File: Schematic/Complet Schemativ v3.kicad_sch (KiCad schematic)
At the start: 49 parts, among them J1 Conn_Coaxial, J2 USB_A, J3 AudioJack3, U1 Si5351A-B-GT, U2 SN74CBT3253, U3 OPAMP, U4 OPAMP, U5 OPAMP, U6 OPAMP

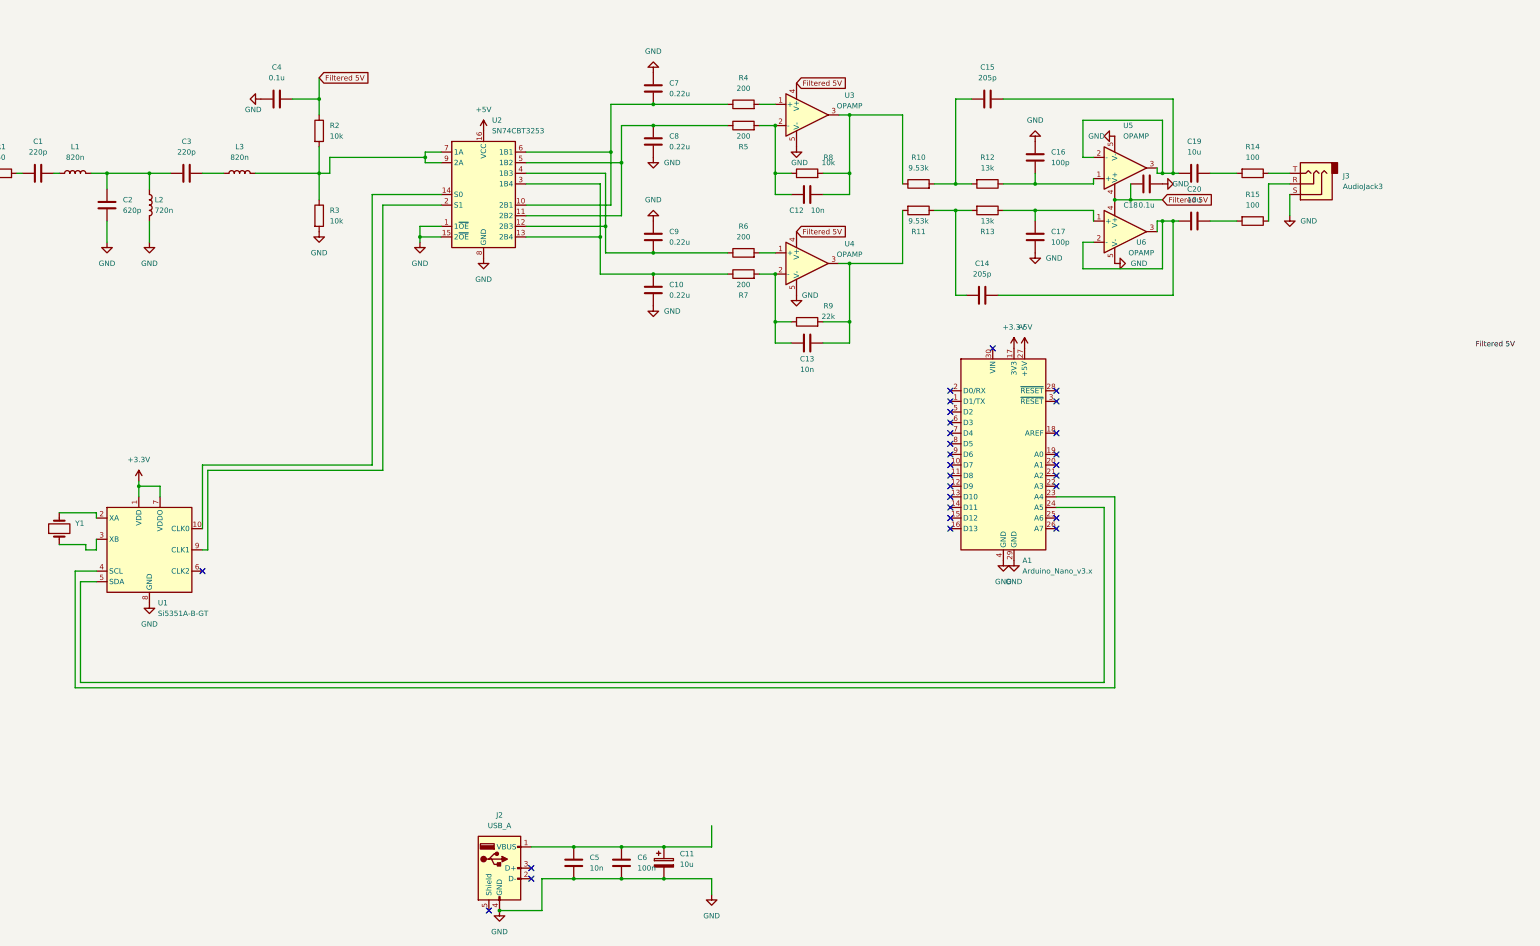
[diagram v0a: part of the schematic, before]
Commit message: Added bypass capacitors to our schematic
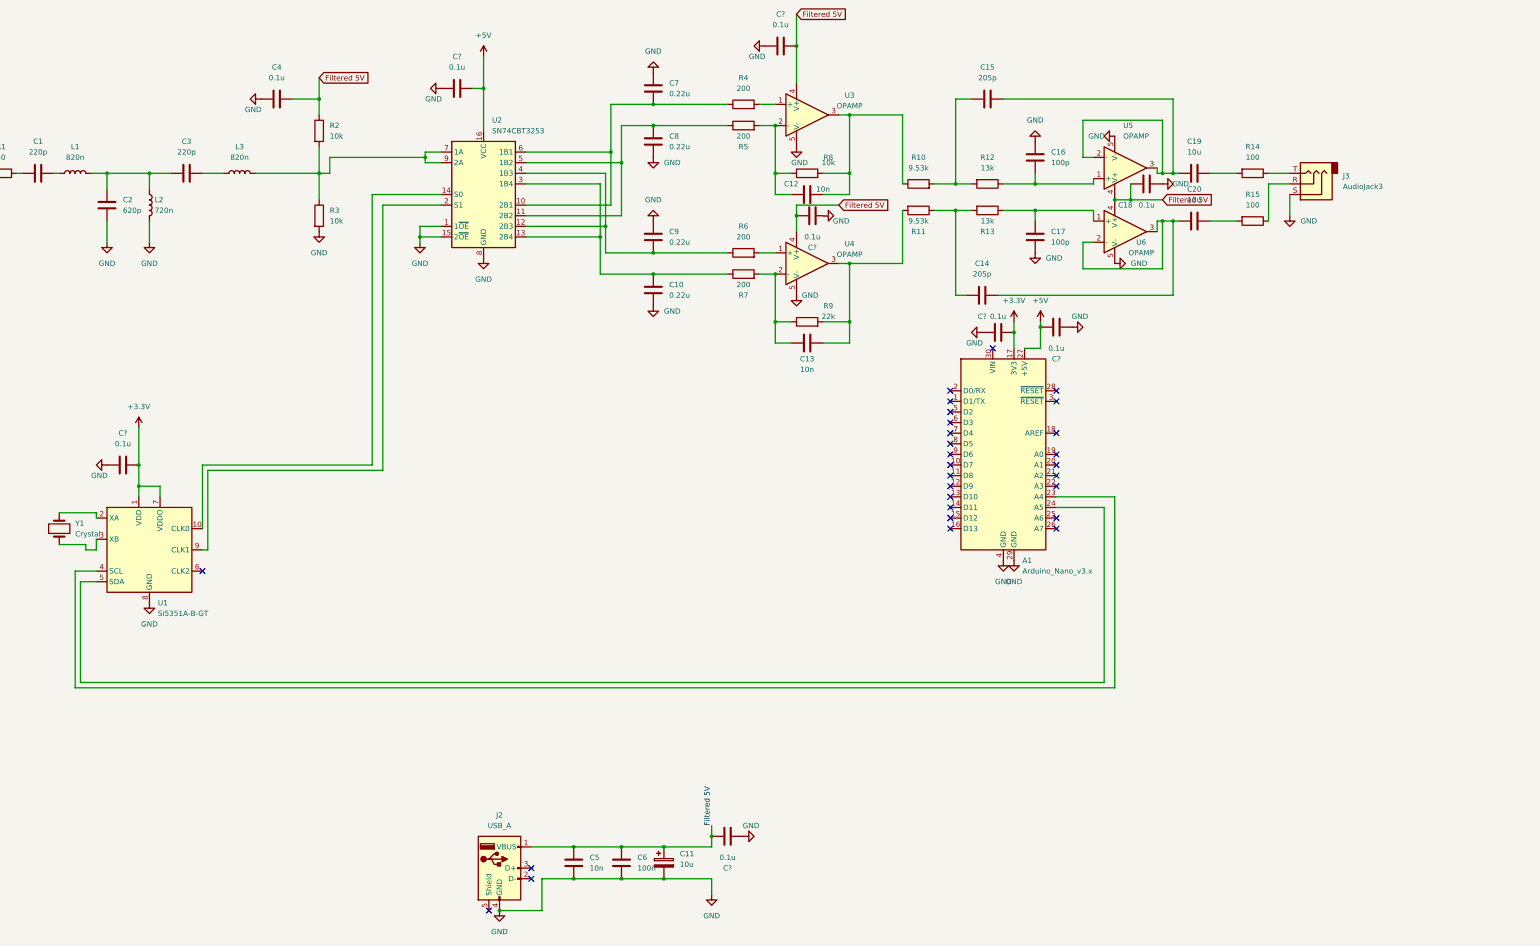
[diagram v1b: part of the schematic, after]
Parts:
- added C? (x7): 0.1u, symbol Device:C
- Y1: value (none) -> Crystal
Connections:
- net +3V3: now also C?.2, C?.2
- net +5V: now also C?.2, C?.2
- net Filtered 5V: now also C11.1, C5.1, C6.1, J2.1 (VBUS), C?.2, C?.2, C?.2
- net GND: now also C?.1, C?.1, C?.1, C?.1, C?.1, C?.1, C?.1

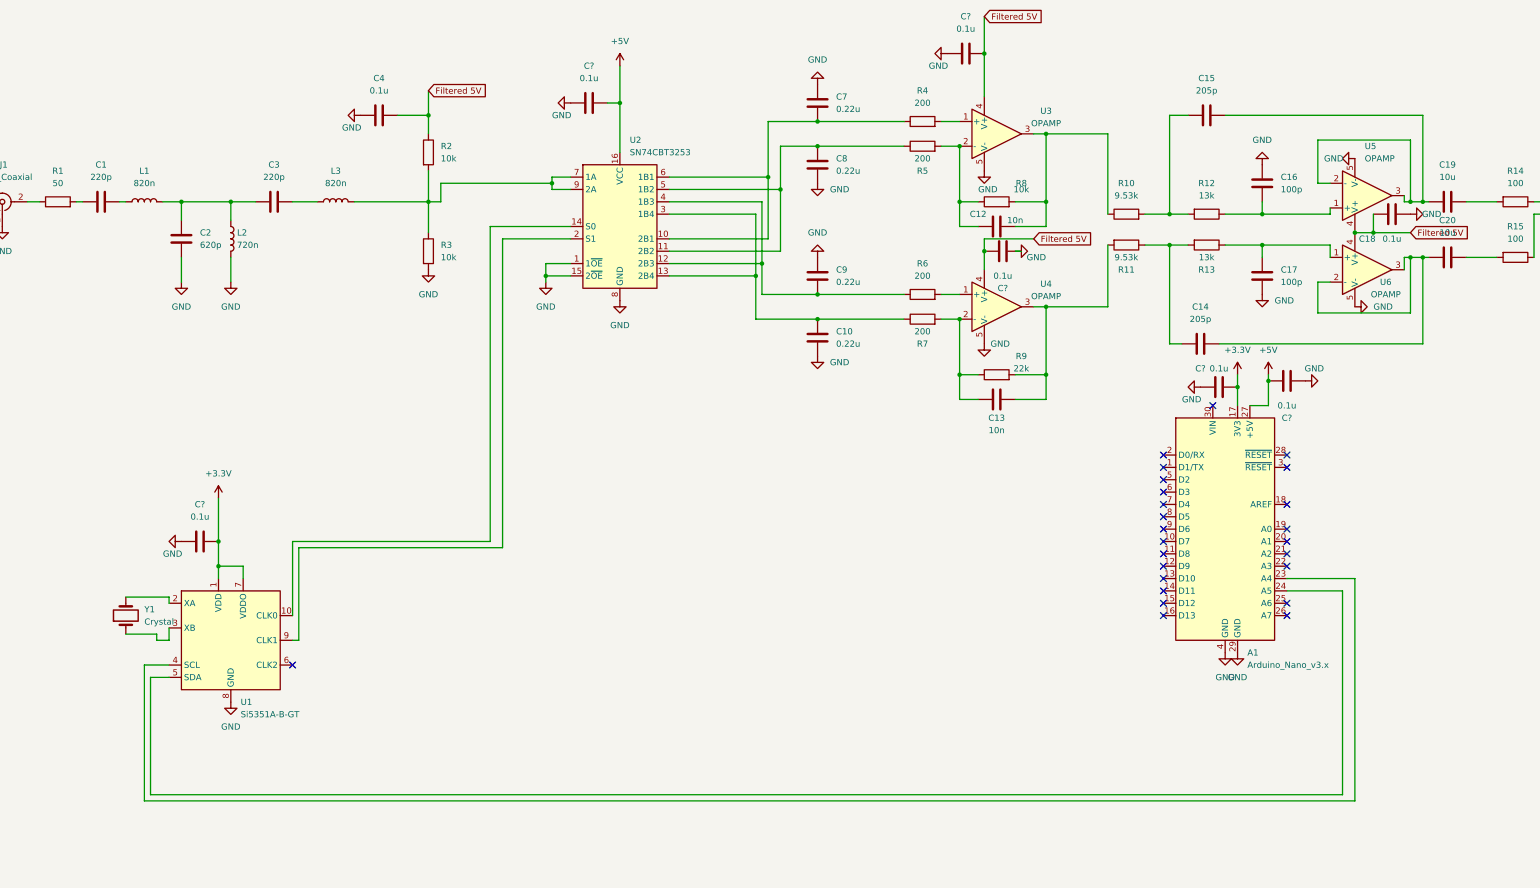
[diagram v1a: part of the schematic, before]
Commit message: Added pull up resistors, bypass capacitors, split the gain between our amplifiers, and changes our bypass filter to 7-18 Mhz
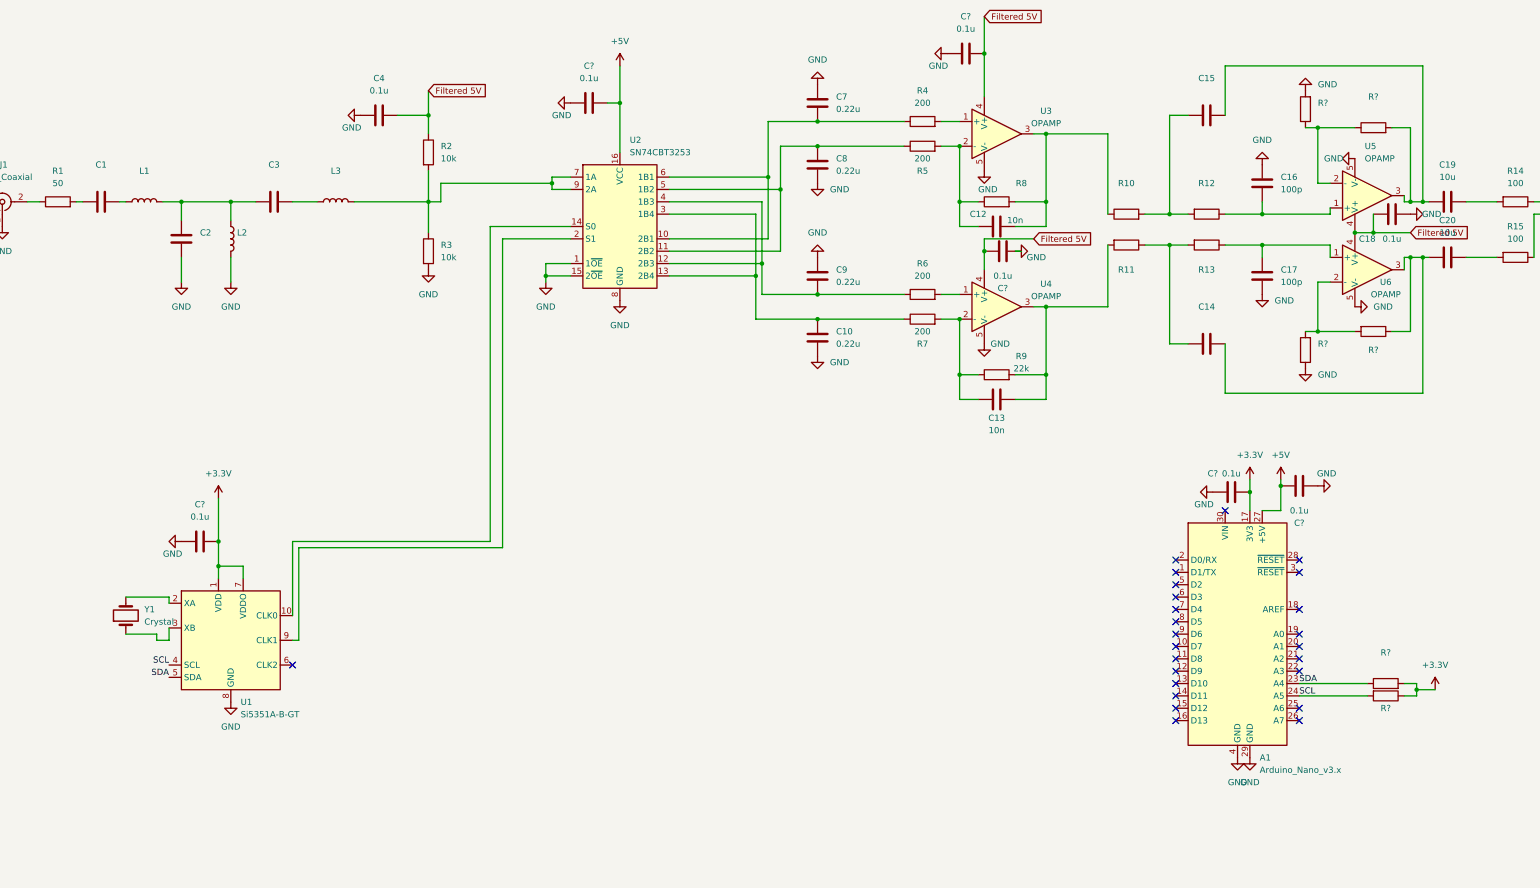
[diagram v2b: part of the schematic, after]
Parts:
- added R? (x6): (no value), symbol Device:R
- C1, C3: value 220p -> (none)
- C14, C15: value 205p -> (none)
- C2: value 620p -> (none)
- L1, L3: value 820n -> (none)
- L2: value 720n -> (none)
- R10, R11: value 9.53k -> (none)
- R12, R13: value 13k -> (none)
- R8: value 10k -> (none)
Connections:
- net +3V3: now also R?.1, R?.2
- net GND: now also R?.1, R?.2
- net at C15.2, C19.2, U5.3: now also R?.2; no longer U5.2 (-)
- net at C14.2, C20.2, U6.3: now also R?.1; no longer U6.2 (-)
- net SCL: now reaches U1.4 (SCL)
- net SCL: now also A1.24 (A5), R?.2; no longer A1.23 (A4)
- net SDA: now reaches U1.5 (SDA)
- net SDA: now also A1.23 (A4), R?.1; no longer A1.24 (A5)
- new net: R?.1, R?.1, U5.2 (-)
- new net: R?.2, R?.2, U6.2 (-)
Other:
- moved on the sheet: A1, C14, C?

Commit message: New Complete Schematic Versions
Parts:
- C1, C3: value (none) -> 270p
- C14, C15: value (none) -> 105p
- C2: value (none) -> 560p
- J2: footprint (none) -> Connector_USB:USB_A_Molex_67643_Horizontal
- L1, L3: value (none) -> 750n
- L2: value (none) -> 360n
- R10, R11: value (none) -> 4.64k
- R12, R13: value (none) -> 52.3k
- R16, R17: renamed from R?; value (none) -> 2.49k
- R18, R19: renamed from R?; value (none) -> 17.4k
- R20, R21: renamed from R?; value (none) -> 4.7k
- R8: value (none) -> 22k
- gave numbers to parts that had none: 7
